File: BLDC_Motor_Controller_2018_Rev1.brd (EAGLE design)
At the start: 112.4 x 80 mm, 143 parts, among them J3 APP_2POS_CONFIG5V_HORIZ, Q1 MOSFET-NCHANNELFQP30N06L, Q2 MOSFET-NCHANNELFQP30N06L, Q3 MOSFET-NCHANNELFQP30N06L, Q4 MOSFET-NCHANNELFQP30N06L, Q5 MOSFET-NCHANNELFQP30N06L, Q6 MOSFET-NCHANNELFQP30N06L, Q7 MOSFET-PCHANNEL, Q8 MOSFET-PCHANNEL, Q9 MOSFET-NCHANNELAO3404A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

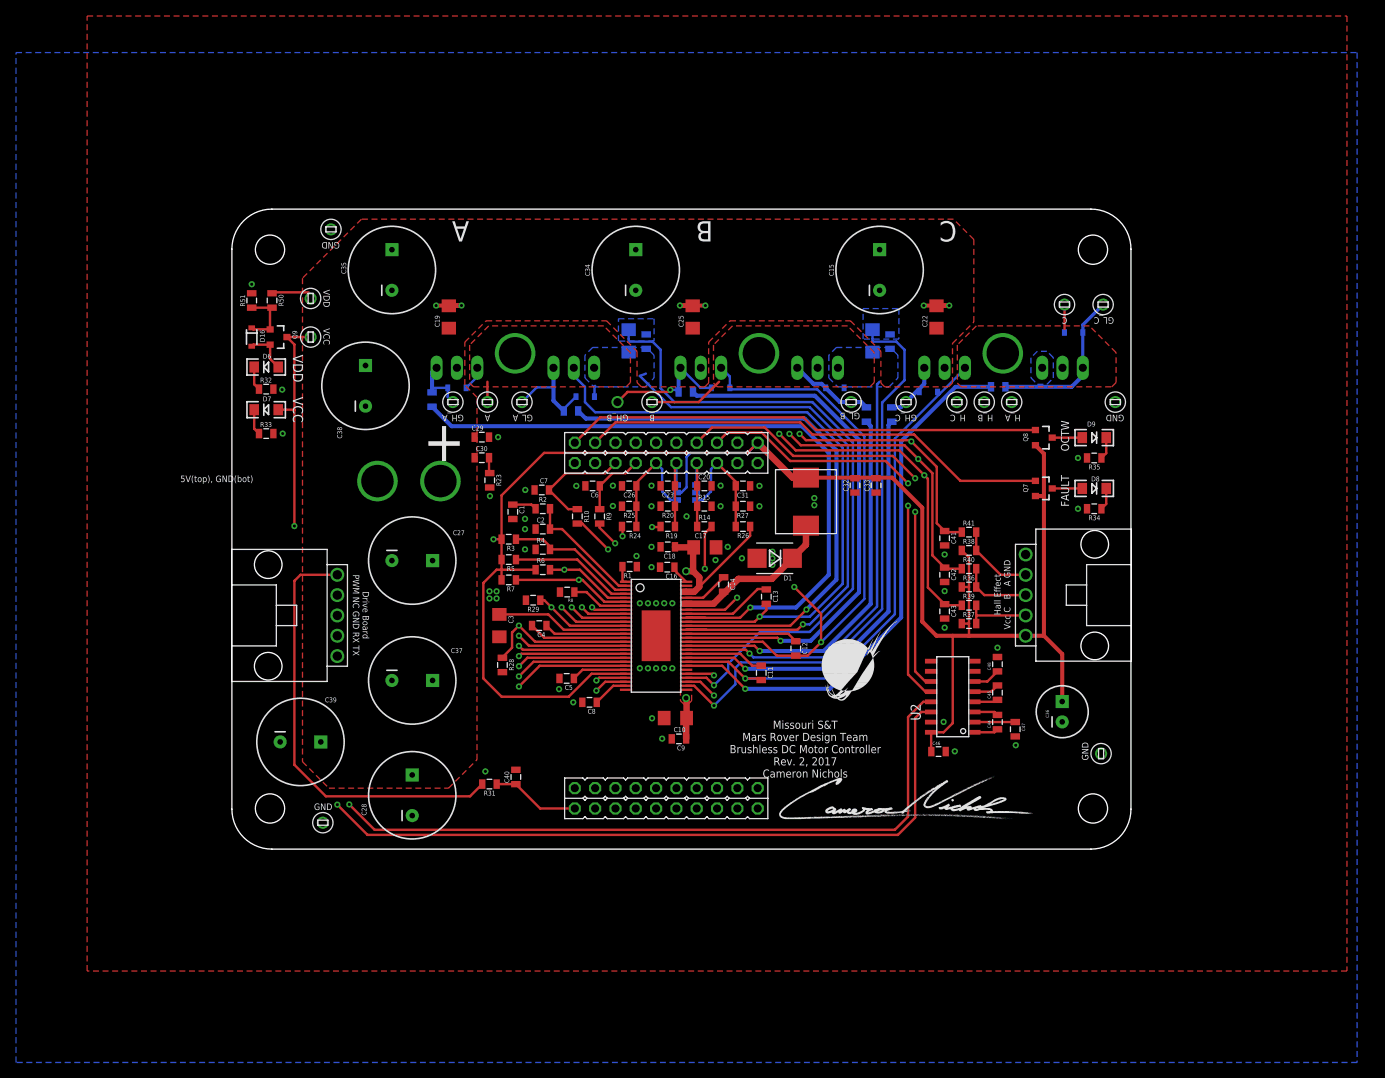
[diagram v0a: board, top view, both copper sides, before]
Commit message: Deleted hall effect hardware, four 220uF caps
Reusing board for 2018 rover but deleting hall effect hardware, deleted four 220uF power conditioning caps and changed remaining caps to 470uF. Added 3pin SL to carry PWM signal to control card without passing through a filter. Changed names of the files to include 2018.
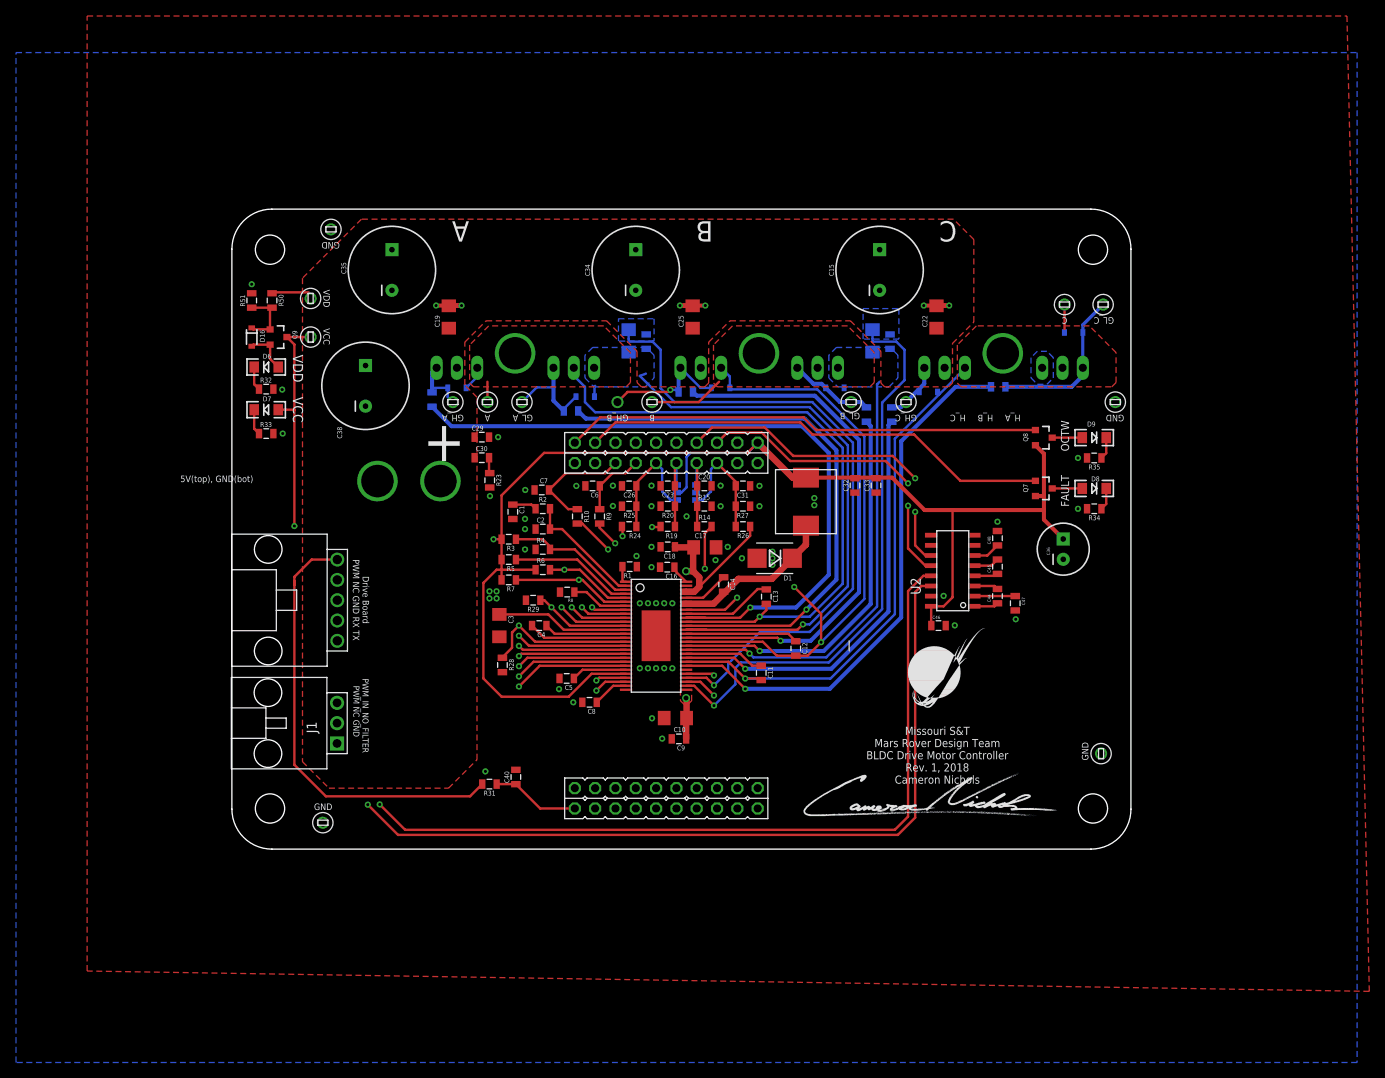
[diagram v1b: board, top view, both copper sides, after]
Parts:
- removed C27, C28, C37, C39: 220u, SparkFun-Passives:CPOL-RADIAL-1000UF-25V
- removed C41, C42, C43: .015u, SparkFun-Passives:0805
- removed R36, R37, R38: 10k, SparkFun-Passives:0805
- removed R39, R40, R41: 10, SparkFun-Passives:0805
- removed U$21, U$22, U$23: TEST_POINT_0.1INDIAM, MRDT-Connectors:TEST_POINT_0.1INDIAM
- removed U$8: 5PIN, Molex-SL:5PIN
- added J1: SL03THROUGH_HOLE, MRDT-Connectors:MOLEX_SL_03_TH
- C15, C34, C35, C38: value 220u -> 470u
- moved C36 20.3 mm to (101.7, 36.2)
- moved C44 15.7 mm to (93.5, 30.4)
- moved C45 15.7 mm to (93.5, 34.0)
- moved C46 15.7 mm to (86.1, 26.7)
- moved C47 15.7 mm to (95.7, 29.5)
- moved C48 15.7 mm to (93.5, 37.6)
- moved U2 15.7 mm to (87.9, 33.5)
- moved U$9 10.8 mm to (82.3, 15.5)
- moved U$4 1.90 mm to (11.0, 29.8)
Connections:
- removed net HALL_A: C41.1, R41.1, U$2.PA5, U$22.P$1
- removed net HALL_B: C42.1, R40.1, U$2.PE5, U$21.P$1
- removed net HALL_C: C43.1, R39.1, U$2.PB5, U$23.P$1
- removed net N$20: R37.2, R39.2, U$8.2
- removed net N$33: R36.2, R40.2, U$8.3
- removed net N$39: R38.2, R41.2, U$8.4
- new net PWM_IN_NO_FILTER: J1.3, U$2.PF4
- net GND: now also J1.1; no longer C27.2, C28.2, C37.2, C39.2, C41.2, C42.2, C43.2, U$8.5
- net PVDD: no longer C27.1, C28.1, C37.1, C39.1
- net VCC: no longer R36.1, R37.1, R38.1, U$8.1
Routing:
- net HALL_B: track 64.7 -> 0.00 mm, vias 2 -> 0
- net HALL_C: track 62.4 -> 0.00 mm, vias 2 -> 0
- net HALL_A: track 61.9 -> 0.00 mm, vias 2 -> 0
- net VCC: track 309.8 -> 261.7 mm
- net PWM_IN_NO_FILTER: track 0.00 -> 34.1 mm
- net UART_TX: track 57.4 -> 41.6 mm
- net UART_RX: track 54.7 -> 38.9 mm
- net 232_TX: track 108.0 -> 123.4 mm
- net 232_RX: track 109.7 -> 125.1 mm
- net N$39: track 9.73 -> 0.00 mm
- net N$33: track 8.89 -> 0.00 mm
- net N$20: track 8.47 -> 0.00 mm
- net N$34: track 54.4 -> 56.0 mm
- net GND: vias 64 -> 61
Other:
- board text added: "Missouri S&T Mars Rover Design Team BLDC Drive Motor Controller Rev. 1, 2018 Cameron Nichols"
- board text added: "PWM_IN_NO_FILTER PWM NC GND"
- board text removed: "Hall Effect Vcc C B A GND"
- board text removed: "Missouri S&T Mars Rover Design Team Brushless DC Motor Controller Rev. 2, 2017 Cameron Nichols"

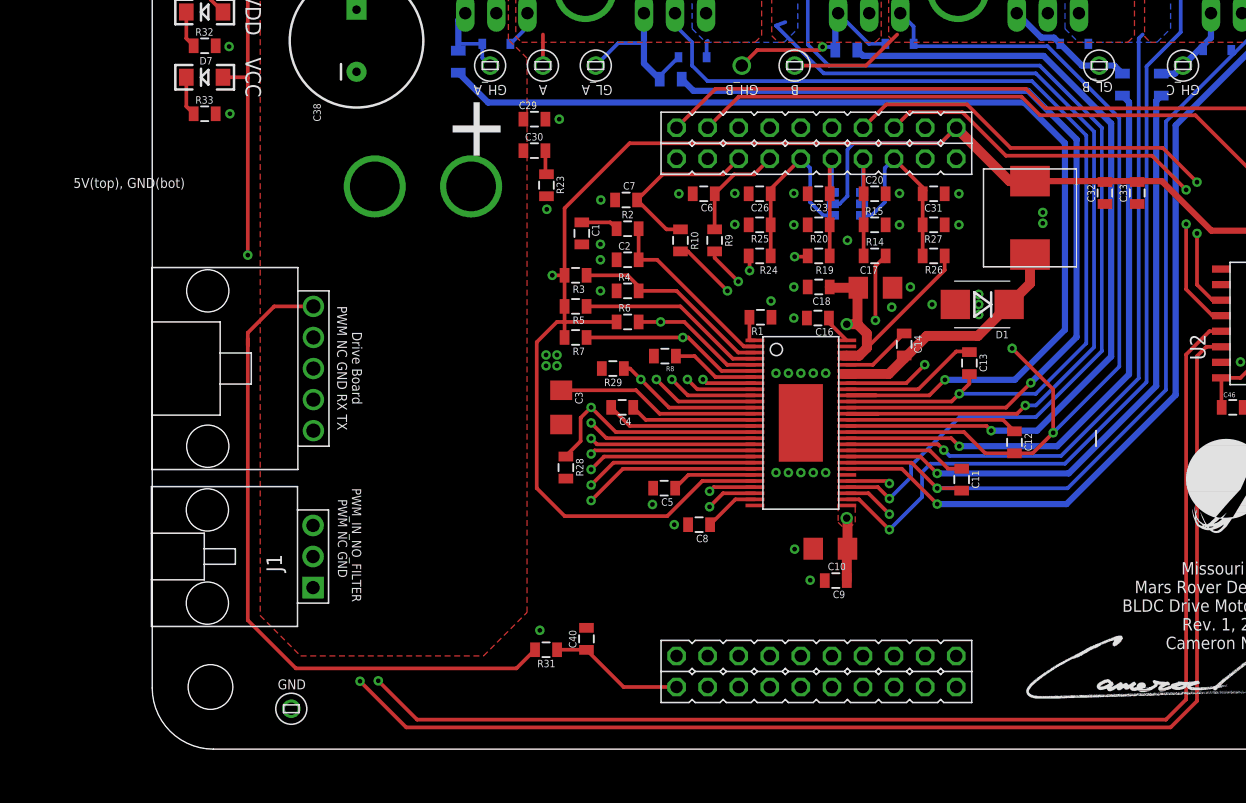
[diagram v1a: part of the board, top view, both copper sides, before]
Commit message: Swapped position of Power andersons and Drive board SL
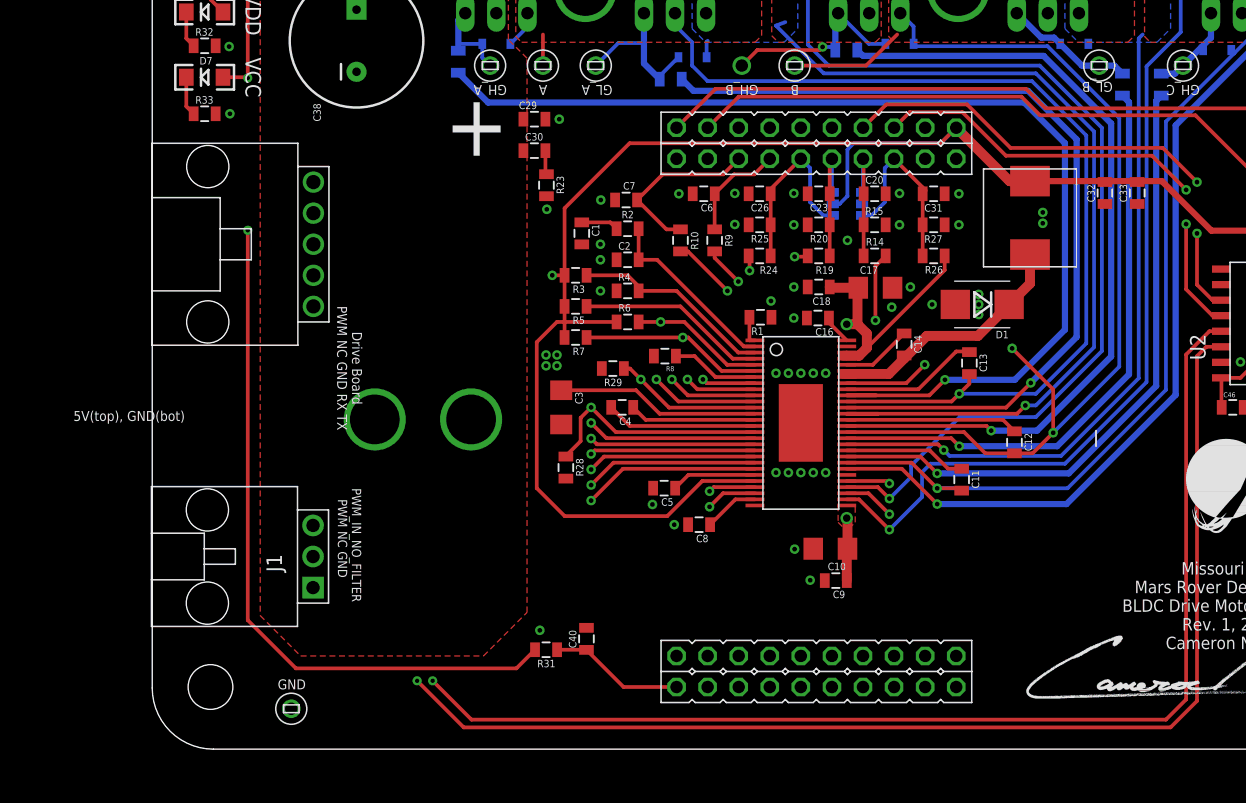
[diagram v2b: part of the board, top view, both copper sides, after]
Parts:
- moved J3 19.0 mm to (-12.2, 21.7)
- moved U$4 10.2 mm to (11.0, 40.0)
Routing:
- net N$34: track 56.0 -> 64.6 mm, vias 0 -> 1
- net VCC: track 261.7 -> 253.2 mm
- net 232_RX: track 125.1 -> 132.6 mm
- net 232_TX: track 123.4 -> 130.9 mm
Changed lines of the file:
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@@
 <?xml version="1.0" encoding="utf-8"?>
 <!DOCTYPE eagle SYSTEM "eagle.dtd">
-<eagle version="8.3.1">
+<eagle version="8.4.3">
 <drawing>
 <settings>
@@
 <setting verticaltext="up"/>
 </settings>
-<grid distance="0.05" unitdist="inch" unit="inch" style="lines" multiple="1" display="yes" altdistance="0.005" altunitdist="inch" altunit="inch"/>
+<grid distance="0.005" unitdist="inch" unit="inch" style="lines" multiple="1" display="yes" altdistance="0.005" altunitdist="inch" altunit="inch"/>
 <layers>
 <layer number="1" name="Top" color="4" fill="1" visible="yes" active="yes"/>
@@
 <param name="dpMaxLengthDifference" value="10mm"/>
 <param name="dpGapFactor" value="2.5"/>
-<param name="checkGrid" value="0"/>
 <param name="checkAngle" value="0"/>
 <param name="checkFont" value="1"/>
 <param name="checkRestrict" value="1"/>
+<param name="checkStop" value="0"/>
 <param name="useDiameter" value="13"/>
 <param name="maxErrors" value="50"/>
@@
 </element>
 <element name="U$9" library="MRDT-Hardware" package="MRDT_LOGO" value="" x="82.2706" y="15.5448"/>
-<element name="J3" library="MRDT-Connectors" package="APP45_5V_HORIZ_CONFIG" value="APP_2POS_CONFIG5V_HORIZ" x="-12.22375" y="40.79875">
-<attribute name="COLOR1" value="RED" x="-12.22375" y="40.79875" size="1.778" layer="27" display="off"/>
-<attribute name="COLOR2" value="BLACK" x="-12.22375" y="40.79875" size="1.778" layer="27" display="off"/>
+<element name="J3" library="MRDT-Connectors" package="APP45_5V_HORIZ_CONFIG" value="APP_2POS_CONFIG5V_HORIZ" x="-12.22375" y="21.74875">
+<attribute name="COLOR1" value="RED" x="-12.22375" y="21.74875" size="1.778" layer="27" display="off"/>
+<attribute name="COLOR2" value="BLACK" x="-12.22375" y="21.74875" size="1.778" layer="27" display="off"/>
 </element>
 <element name="C38" library="SparkFun-Passives" package="CPOL-RADIAL-1000UF-25V" value="470u" x="14.478" y="56.642" smashed="yes" rot="R90">
@@
 <attribute name="VALUE" x="18.796" y="54.737" size="0.8128" layer="27" rot="R90"/>
 </element>
-<element name="U$4" library="Molex-SL" package="5PIN" value="5PIN" x="10.95375" y="29.845" rot="R90"/>
+<element name="U$4" library="Molex-SL" package="5PIN" value="5PIN" x="10.95375" y="40.005" rot="R90"/>
 <element name="SH1" library="BLDC_Motor_Controller_2016_Rev1" package="SHORT_TOP-50" value="SHORT-HT5" x="77.851" y="62.32525" smashed="yes" rot="MR270">
 <attribute name="BOM" value="no" x="77.851" y="62.32525" size="1.778" layer="28" rot="MR270" display="off"/>
@@
 <wire x1="31.485" y1="34.925" x2="31.485" y2="33.655" width="0.3048" layer="1"/>
 <wire x1="99.28225" y1="42.926" x2="99.28225" y2="48.1515" width="0.508" layer="1"/>
-<wire x1="5.588" y1="61.806" x2="5.588" y2="53.594" width="0.3048" layer="1"/>
-<wire x1="5.588" y1="53.594" x2="5.588" y2="39.116" width="0.3048" layer="1"/>
 <contactref element="Q9" pad="3"/>
 <wire x1="4.656" y1="62.738" x2="5.588" y2="61.806" width="0.3048" layer="1"/>
 <contactref element="U$10" pad="P$1"/>
 <wire x1="7.62" y1="62.738" x2="4.656" y2="62.738" width="0.3048" layer="1"/>
-<wire x1="3.56375" y1="53.6575" x2="5.5245" y2="53.6575" width="0.3048" layer="1"/>
-<wire x1="5.5245" y1="53.6575" x2="5.588" y2="53.594" width="0.3048" layer="1"/>
 <contactref element="U1" pad="5"/>
 <wire x1="53.4162" y1="43.307" x2="53.975" y2="43.307" width="0.3048" layer="16"/>
@@
 <wire x1="85.184" y1="29.083" x2="86.741" y2="29.083" width="0.3048" layer="1"/>
 <wire x1="86.741" y1="29.083" x2="87.884" y2="30.226" width="0.3048" layer="1"/>
-<via x="5.588" y="39.116" extent="1-16" drill="0.381"/>
 <wire x1="31.485" y1="37.465" x2="30.48" y2="37.465" width="0.3048" layer="1"/>
 <via x="30.48" y="37.465" extent="1-16" drill="0.381"/>
-<wire x1="30.48" y1="37.465" x2="7.239" y2="37.465" width="0.3048" layer="15"/>
-<wire x1="7.239" y1="37.465" x2="5.588" y2="39.116" width="0.3048" layer="15"/>
 <wire x1="47.05" y1="20.65" x2="42.748" y2="20.65" width="0.3048" layer="1"/>
 <wire x1="42.748" y1="20.65" x2="39.878" y2="17.78" width="0.3048" layer="1"/>
@@
 <wire x1="87.884" y1="30.226" x2="87.8592875" y2="30.2507125" width="0.3048" layer="1"/>
 <wire x1="87.8592875" y1="30.2507125" x2="87.8592875" y2="41.11510625" width="0.3048" layer="1"/>
+<wire x1="5.588" y1="61.806" x2="5.588" y2="53.594" width="0.3048" layer="1"/>
+<via x="5.588" y="53.594" extent="1-16" drill="0.35"/>
+<wire x1="21.717" y1="37.465" x2="30.48" y2="37.465" width="0.3048" layer="15"/>
+<wire x1="5.588" y1="53.594" x2="21.717" y2="37.465" width="0.3048" layer="15"/>
+<wire x1="5.588" y1="53.594" x2="5.5245" y2="53.6575" width="0.3048" layer="1"/>
+<wire x1="5.5245" y1="53.6575" x2="3.56375" y2="53.6575" width="0.3048" layer="1"/>
 </signal>
 <signal name="N$5">
@@
 <wire x1="85.184" y1="32.893" x2="84.201" y2="32.893" width="0.3048" layer="1"/>
 <wire x1="82.296" y1="30.988" x2="84.201" y2="32.893" width="0.3048" layer="1"/>
-<wire x1="19.431" y1="1.143" x2="80.645" y2="1.143" width="0.3048" layer="1"/>
-<via x="16.256" y="4.318" extent="1-16" drill="0.381"/>
-<wire x1="16.256" y1="4.318" x2="19.431" y2="1.143" width="0.3048" layer="1"/>
 <wire x1="80.645" y1="1.143" x2="82.296" y2="2.794" width="0.3048" layer="1"/>
 <wire x1="82.296" y1="2.794" x2="82.296" y2="30.988" width="0.3048" layer="1"/>
-<wire x1="16.256" y1="22.00275" x2="10.95375" y2="27.305" width="0.3048" layer="15"/>
-<wire x1="16.256" y1="4.318" x2="16.256" y2="22.00275" width="0.3048" layer="15"/>
+<wire x1="10.95375" y1="37.465" x2="20.701" y2="27.71775" width="0.3048" layer="15"/>
+<wire x1="20.701" y1="27.71775" x2="20.701" y2="4.318" width="0.3048" layer="15"/>
+<via x="20.701" y="4.318" extent="1-16" drill="0.35"/>
+<wire x1="20.701" y1="4.318" x2="23.876" y2="1.143" width="0.3048" layer="1"/>
+<wire x1="23.876" y1="1.143" x2="80.645" y2="1.143" width="0.3048" layer="1"/>
 </signal>
 <signal name="232_TX">
@@
 <wire x1="85.184" y1="31.623" x2="83.947" y2="31.623" width="0.3048" layer="1"/>
 <wire x1="83.185" y1="30.861" x2="83.947" y2="31.623" width="0.3048" layer="1"/>
-<wire x1="18.542" y1="0.508" x2="81.026" y2="0.508" width="0.3048" layer="1"/>
-<via x="14.76375" y="4.28625" extent="1-16" drill="0.381"/>
-<wire x1="14.76375" y1="4.28625" x2="18.542" y2="0.508" width="0.3048" layer="1"/>
 <wire x1="81.026" y1="0.508" x2="83.185" y2="2.667" width="0.3048" layer="1"/>
 <wire x1="83.185" y1="2.667" x2="83.185" y2="30.861" width="0.3048" layer="1"/>
-<wire x1="14.76375" y1="4.28625" x2="14.76375" y2="20.955" width="0.3048" layer="15"/>
-<wire x1="14.76375" y1="20.955" x2="10.95375" y2="24.765" width="0.3048" layer="15"/>
+<wire x1="10.95375" y1="34.925" x2="19.431" y2="26.44775" width="0.3048" layer="15"/>
+<wire x1="19.431" y1="26.44775" x2="19.431" y2="4.318" width="0.3048" layer="15"/>
+<via x="19.431" y="4.318" extent="1-16" drill="0.35"/>
+<wire x1="19.431" y1="4.318" x2="23.241" y2="0.508" width="0.3048" layer="1"/>
+<wire x1="23.241" y1="0.508" x2="81.026" y2="0.508" width="0.3048" layer="1"/>
 </signal>
 <signal name="UART_RX">
@@
 <contactref element="R31" pad="2"/>
 <contactref element="U$4" pad="1"/>
-<wire x1="5.588" y1="32.258" x2="5.588" y2="31.75" width="0.3048" layer="1"/>
-<wire x1="5.588" y1="31.75" x2="5.588" y2="9.271" width="0.3048" layer="1"/>
-<wire x1="5.588" y1="9.271" x2="9.525" y2="5.334" width="0.3048" layer="1"/>
+<wire x1="9.525" y1="5.334" x2="5.588" y2="9.271" width="0.3048" layer="1"/>
 <wire x1="9.525" y1="5.334" x2="27.548" y2="5.334" width="0.3048" layer="1"/>
 <wire x1="27.548" y1="5.334" x2="29.072" y2="6.858" width="0.3048" layer="1"/>
-<wire x1="5.588" y1="31.75" x2="5.588" y2="32.766" width="0.3048" layer="1"/>
-<wire x1="5.588" y1="32.766" x2="7.747" y2="34.925" width="0.3048" layer="1"/>
-<wire x1="7.747" y1="34.925" x2="10.95375" y2="34.925" width="0.3048" layer="1"/>
+<wire x1="5.588" y1="9.271" x2="5.588" y2="41.148" width="0.3048" layer="1"/>
+<via x="5.588" y="41.148" extent="1-16" drill="0.35"/>
+<wire x1="5.588" y1="41.148" x2="9.525" y2="45.085" width="0.3048" layer="15"/>
+<wire x1="9.525" y1="45.085" x2="10.95375" y2="45.085" width="0.3048" layer="15"/>
 </signal>
 <signal name="+5V">
